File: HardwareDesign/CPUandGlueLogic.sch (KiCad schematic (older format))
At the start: 31 parts, among them J100 Conn_02x40_Counter_Clockwise, U100 74HCT245, U101 74HCT245, U102 MAX708, U103 HD6809, U104 74HCT245, U105 74HCT365, U106 74HCT00, U107 74HCT27, U108 74HCT138, U109 74HCT138, U110 74HCT138, Y100 Crystal

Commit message: added bulk decoupling cap for CPU+glue logic board
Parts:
- added C112: 10μF, symbol device:CP
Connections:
- net labels added: PC8
- wire segments 420 -> 422
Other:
- note added: "Bulk decoupling for board,\nplace near power pins of\n2x40 connector to backplane"
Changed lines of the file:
@@
 Text Label 7500 7050 0    50   ~ 0
 PC7
+Text Label 7500 7150 0    50   ~ 0
+PC8
+$Comp
+L device:CP C112
+U 1 1 61CF6F76
+P 5850 5150
+F 0 "C112" H 5968 5196 50  0000 L CNN
+F 1 "10μF" H 5968 5105 50  0000 L CNN
+F 2 "" H 5888 5000 50  0001 C CNN
+F 3 "" H 5850 5150 50  0001 C CNN
+	1    5850 5150
+	1    0    0    -1
+$EndComp
+Wire Wire Line
+	5850 5000 5850 4850
+$Comp
+L power:VCC #PWR?
+U 1 1 61D33C29
+P 5850 4850
+F 0 "#PWR?" H 5850 4700 50  0001 C CNN
+F 1 "VCC" H 5867 5023 50  0000 C CNN
+F 2 "" H 5850 4850 50  0001 C CNN
+F 3 "" H 5850 4850 50  0001 C CNN
+	1    5850 4850
+	1    0    0    -1
+$EndComp
+Wire Wire Line
+	5850 5300 5850 5500
 Wire Bus Line
 	1000 5700 3650 5700
@@
 Wire Bus Line
 	2450 6150 2450 9200
+$Comp
+L power:GND #PWR?
+U 1 1 61D6EF92
+P 5850 5500
+F 0 "#PWR?" H 5850 5250 50  0001 C CNN
+F 1 "GND" H 5855 5327 50  0000 C CNN
+F 2 "" H 5850 5500 50  0001 C CNN
+F 3 "" H 5850 5500 50  0001 C CNN
+	1    5850 5500
+	1    0    0    -1
+$EndComp
+Text Notes 6050 4900 0    50   ~ 0
+Bulk decoupling for board,\nplace near power pins of\n2x40 connector to backplane
 $EndSCHEMATC

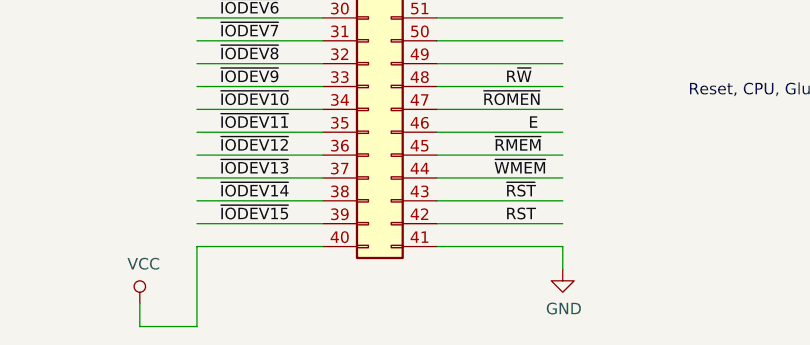
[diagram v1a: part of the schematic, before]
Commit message: label backplane connector
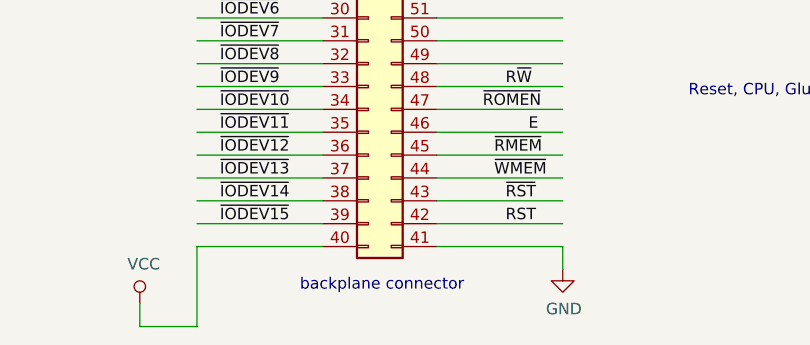
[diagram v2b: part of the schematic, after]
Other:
- note added: "backplane connector"
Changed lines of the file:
@@
 Text Notes 6050 4900 0    50   ~ 0
 Bulk decoupling for board,\nplace near power pins of\n2x40 connector to backplane
+Text Notes 7850 10250 0    50   ~ 0
+backplane connector
 $EndSCHEMATC

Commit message: more work on preparing for PCB design
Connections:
- net labels added: TIRQ
- net labels removed: PC8
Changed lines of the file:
@@
 PC7
 Text Label 7500 7150 0    50   ~ 0
-PC8
+TIRQ
 $Comp
 L device:CP C112
@@
 Wire Wire Line
 	5850 5300 5850 5500
-Wire Bus Line
-	1000 5700 3650 5700
-Wire Bus Line
-	3750 5250 3750 5600
-Wire Bus Line
-	1350 4250 1350 5600
-Wire Bus Line
-	4500 4450 4500 7250
-Wire Bus Line
-	2450 6150 2450 9200
 $Comp
 L power:GND #PWR?
@@
 Text Notes 7850 10250 0    50   ~ 0
 backplane connector
+Wire Bus Line
+	1000 5700 3650 5700
+Wire Bus Line
+	3750 5250 3750 5600
+Wire Bus Line
+	1350 4250 1350 5600
+Wire Bus Line
+	4500 4450 4500 7250
+Wire Bus Line
+	2450 6150 2450 9200
 $EndSCHEMATC

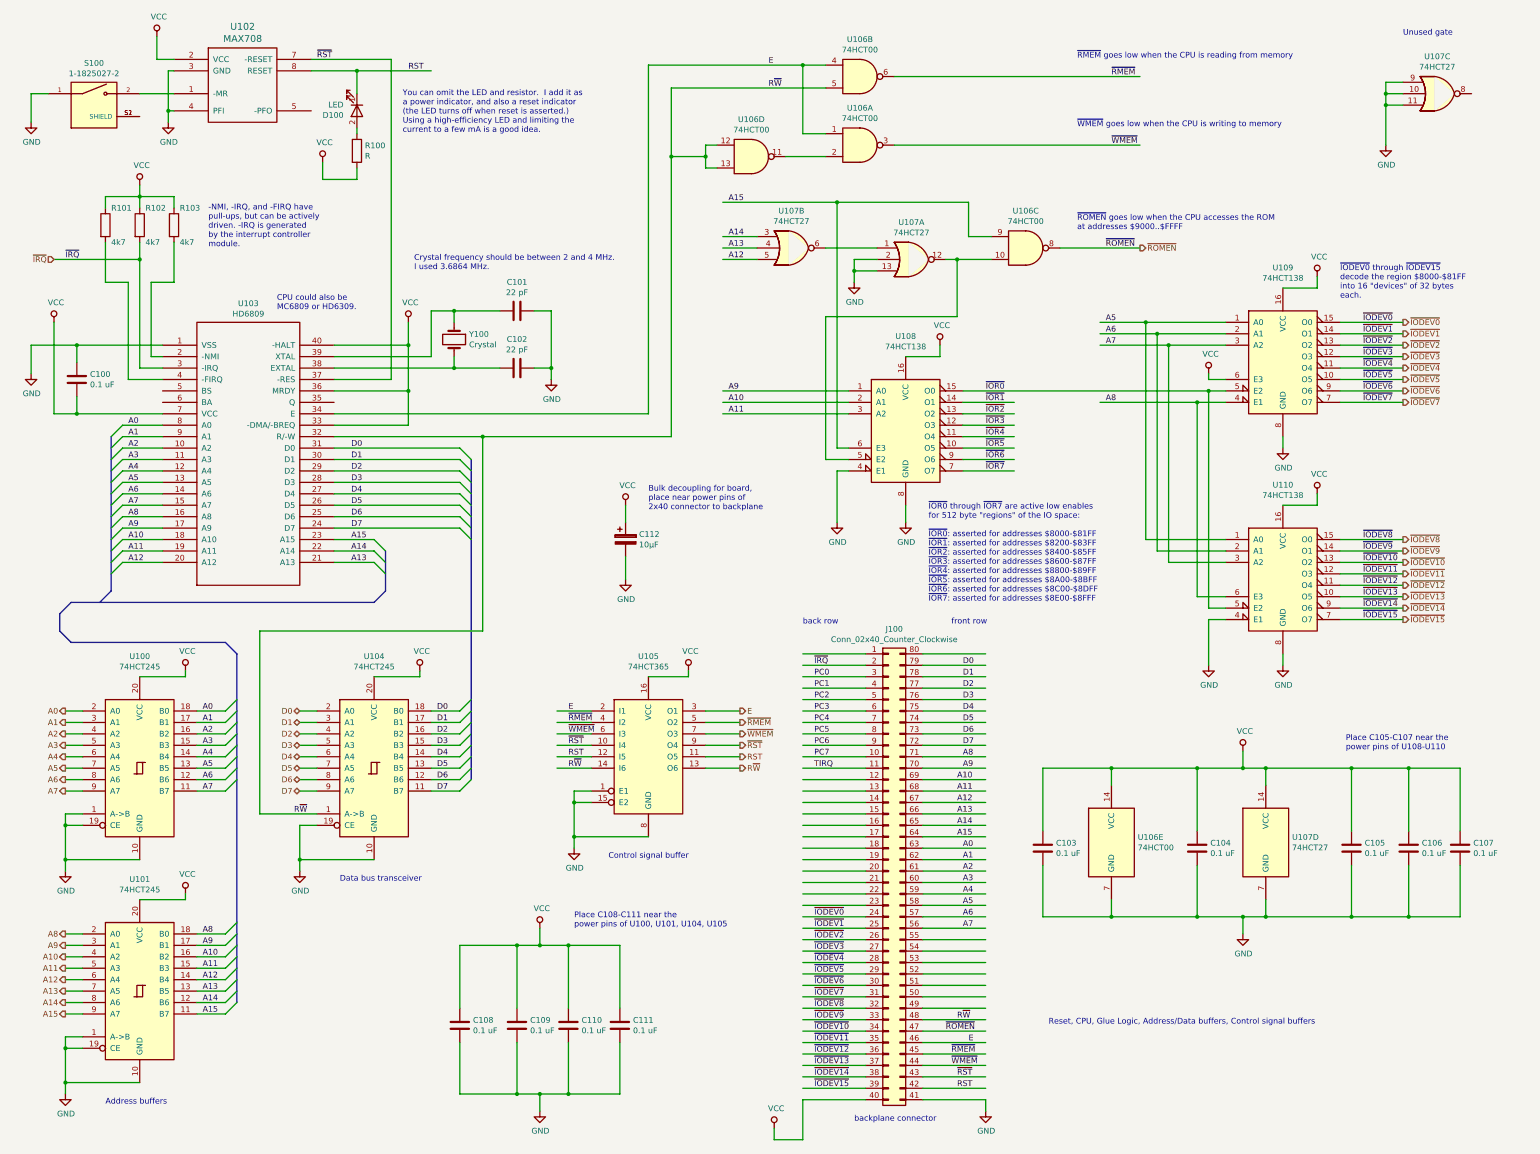
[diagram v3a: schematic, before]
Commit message: more cleanups in preparation for PCB layout
Renamed nets to distinguish unbuffered vs. buffered signals.

Fixed one error in interrupt controller (D0 was tied
to ground.)

Not entirely done yet.
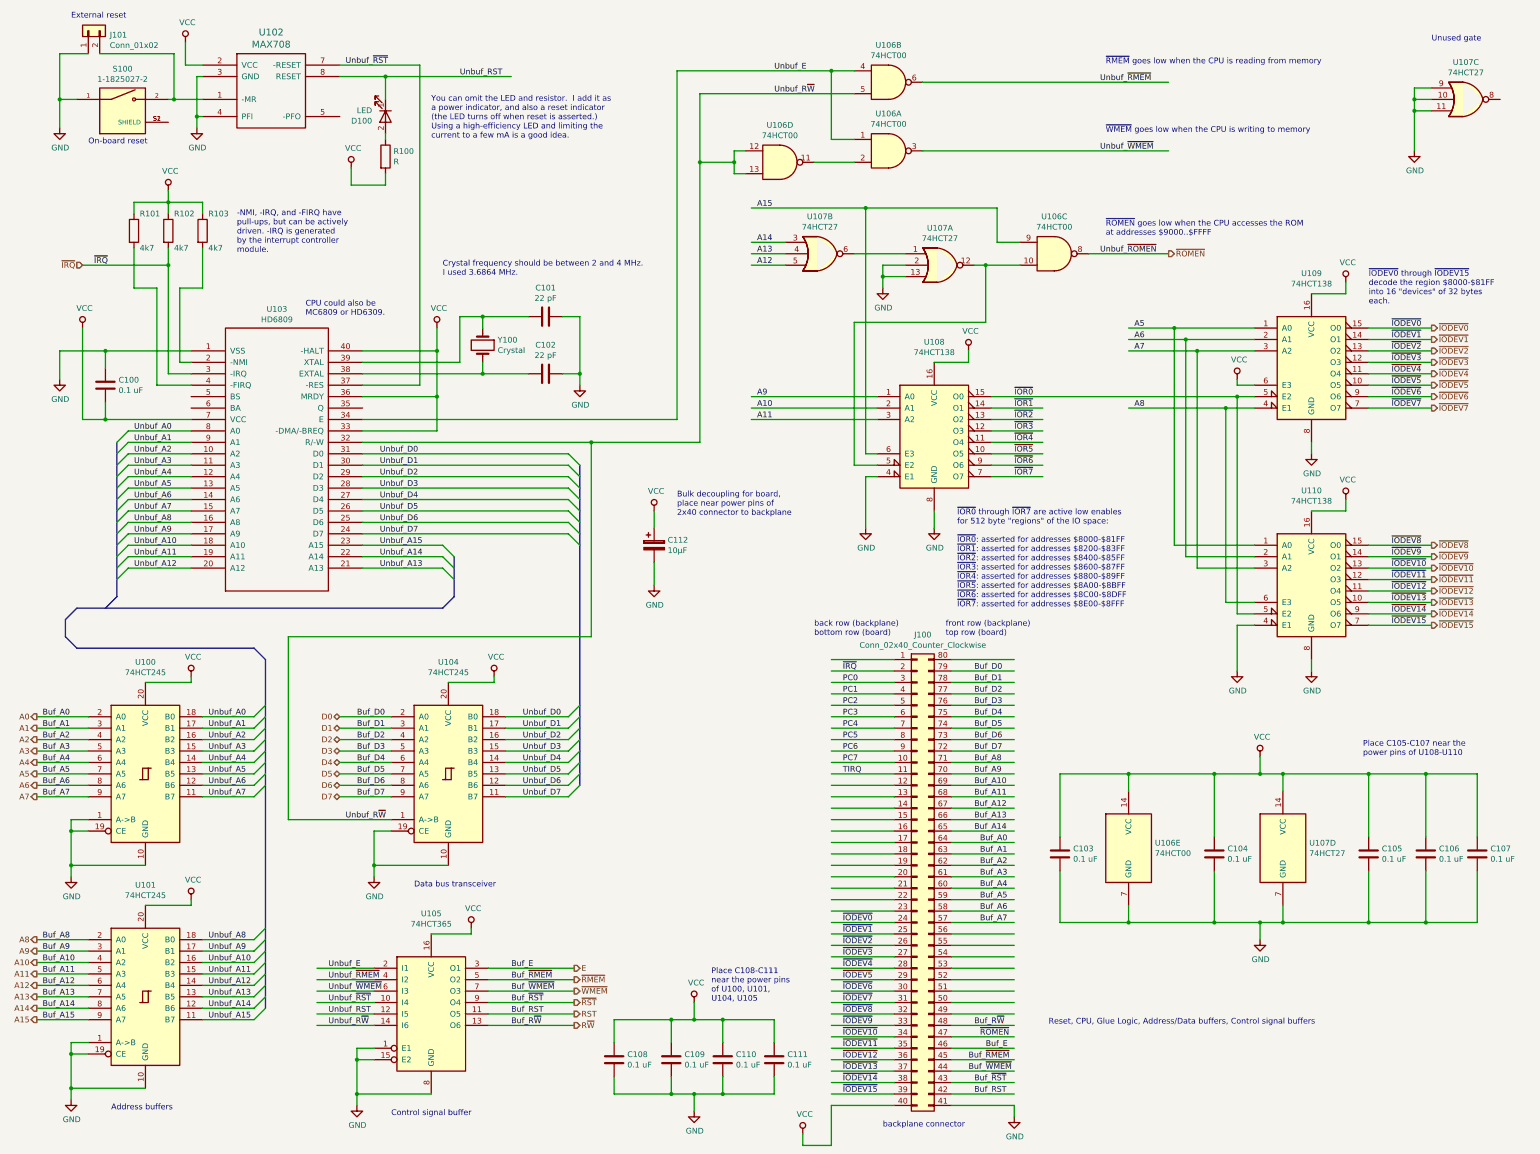
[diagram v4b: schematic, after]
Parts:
- added J101: Conn_01x02, symbol Connector_Generic:Conn_01x02
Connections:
- net labels added: Buf_A0, Buf_A1, Buf_A10, Buf_A11, Buf_A12, Buf_A13, Buf_A14, Buf_A15, Buf_A2, Buf_A3, Buf_A4, Buf_A5, Buf_A6, Buf_A7, Buf_A8, Buf_A9, Buf_D0, Buf_D1, Buf_D2, Buf_D3, Buf_D4, Buf_D5, Buf_D6, Buf_D7, Buf_E, Buf_RST, Buf_R~W~, Buf_~RMEM~, Buf_~RST~, Buf_~WMEM~, Unbuf_A0, Unbuf_A1, Unbuf_A10, Unbuf_A11, Unbuf_A12, Unbuf_A13, Unbuf_A14, Unbuf_A15, Unbuf_A2, Unbuf_A3, Unbuf_A4, Unbuf_A5, Unbuf_A6, Unbuf_A7, Unbuf_A8, Unbuf_A9, Unbuf_D0, Unbuf_D1, Unbuf_D2, Unbuf_D3, Unbuf_D4, Unbuf_D5, Unbuf_D6, Unbuf_D7, Unbuf_E, Unbuf_RST, Unbuf_R~W~, Unbuf_~RMEM~, Unbuf_~ROMEN~, Unbuf_~RST~, Unbuf_~WMEM~
- net labels removed: R~W~, ~RMEM, ~ROMEN, ~WMEM
- wire segments 422 -> 427
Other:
- note added: "External reset"
- note added: "On-board reset"
- note added: "Place C108-C111\nnear the power pins\nof U100, U101,\nU104, U105"
- note added: "back row (backplane)\nbottom row (board)"
- note added: "front row (backplane)\ntop row (board)"
- note removed: "Place C108-C111 near the\npower pins of U100, U101, U104, U105"
- note removed: "back row"
- note removed: "front row"
- moved on the sheet: C100, C101, C102, C103, C104, C105, C106, C107, C108, C109, C110, C111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
